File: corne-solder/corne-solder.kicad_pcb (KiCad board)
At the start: 2 copper layers, 133.8 x 91.7 mm, 49 parts, among them J1 Battery Connector, J2 nice!view, J3 USB_C_Receptacle_PowerOnly_6P, J4 Battery Wire, SW1 SW_Push, SW10 SW_Push, SW11 SW_Push, SW12 SW_Push, SW13 SW_Push, SW14 SW_Push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

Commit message: Update corne-solder.kicad_pcb
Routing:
- net GND: vias 6 -> 21
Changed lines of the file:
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@@
 		(pad_to_mask_clearance 0)
 		(allow_soldermask_bridges_in_footprints no)
-		(grid_origin 155.1 60.05)
+		(grid_origin 50 50)
 		(pcbplotparams
 			(layerselection 0x00010fc_ffffffff)
@@
 	)
 	(via
-		(at 138.5 79.125)
+		(at 126 41.75)
+		(size 0.6)
+		(drill 0.3)
+		(layers "F.Cu" "B.Cu")
+		(net 27)
+	)
+	(via
+		(at 126 79.75)
+		(size 0.6)
+		(drill 0.3)
+		(layers "F.Cu" "B.Cu")
+		(net 27)
+	)
+	(via
+		(at 145 82.125)
+		(size 0.6)
+		(drill 0.3)
+		(layers "F.Cu" "B.Cu")
+		(net 27)
+	)
+	(via
+		(at 50 65.5)
+		(size 0.6)
+		(drill 0.3)
+		(layers "F.Cu" "B.Cu")
+		(net 27)
+	)
+	(via
+		(at 69 65.5)
+		(size 0.6)
+		(drill 0.3)
+		(layers "F.Cu" "B.Cu")
+		(net 27)
+	)
+	(via
+		(at 145 44.125)
+		(size 0.6)
+		(drill 0.3)
+		(layers "F.Cu" "B.Cu")
+		(net 27)
+	)
+	(via
+		(at 145 63.125)
+		(size 0.6)
+		(drill 0.3)
+		(layers "F.Cu" "B.Cu")
+		(net 27)
+	)
+	(via
+		(at 107 39.375)
+		(size 0.6)
+		(drill 0.3)
+		(layers "F.Cu" "B.Cu")
+		(net 27)
+	)
+	(via
+		(at 50 46.5)
 		(size 0.6)
 		(drill 0.3)
@@
 	)
 	(via
-		(at 81.5 57.75)
+		(at 88 60.75)
+		(size 0.6)
+		(drill 0.3)
+		(layers "F.Cu" "B.Cu")
+		(net 27)
+	)
+	(via
+		(at 107 58.375)
+		(size 0.6)
+		(drill 0.3)
+		(layers "F.Cu" "B.Cu")
+		(net 27)
+	)
+	(via
+		(at 88 41.75)
+		(size 0.6)
+		(drill 0.3)
+		(layers "F.Cu" "B.Cu")
+		(net 27)
+	)
+	(via
+		(at 88 79.75)
+		(size 0.6)
+		(drill 0.3)
+		(layers "F.Cu" "B.Cu")
+		(net 27)
+	)
+	(via
+		(at 126 60.75)
+		(size 0.6)
+		(drill 0.3)
+		(layers "F.Cu" "B.Cu")
+		(net 27)
+	)
+	(via
+		(at 107 77.375)
+		(size 0.6)
+		(drill 0.3)
+		(layers "F.Cu" "B.Cu")
+		(net 27)
+	)
+	(via
+		(at 69 84.5)
+		(size 0.6)
+		(drill 0.3)
+		(layers "F.Cu" "B.Cu")
+		(net 27)
+	)
+	(via
+		(at 50 84.5)
 		(size 0.6)
 		(drill 0.3)
@@
 	)
 	(via
-		(at 119.5 57.75)
+		(at 69 46.5)
 		(size 0.6)
 		(drill 0.3)

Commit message: major edit
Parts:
- moved U1 0.63 mm to (164.6, 59.4)
- moved J1 0.63 mm to (162.4, 82.4)
- moved J4 0.32 mm to (157.6, 84.5)
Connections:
- U1 pad 1: unconnected-(U1-D3-TX-Pad1) -> CS
- U1 pad 12: CS -> unconnected-(U1-B5-Pad12)
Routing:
- net CS: track 22.2 -> 53.2 mm, vias 1 -> 2
- net GND: track 78.5 -> 97.8 mm, vias 21 -> 23
- net row2: track 134.7 -> 148.9 mm, vias 0 -> 1
- net row3: track 72.7 -> 86.8 mm, vias 1 -> 2
- net row0: track 121.5 -> 135.2 mm, vias 0 -> 1
- net row1: track 118.2 -> 130.6 mm, vias 0 -> 1
- net SDA: track 42.9 -> 54.5 mm
- net unconnected-(U1-D3-TX-Pad1): track 11.4 -> 0.00 mm, vias 1 -> 0
- net SCL: track 35.7 -> 45.1 mm
- net battery: track 77.1 -> 69.4 mm
- net RAW: track 22.1 -> 16.2 mm
- net VCC: track 59.9 -> 65.5 mm, vias 2 -> 4
- net col3: track 109.9 -> 106.0 mm, vias 0 -> 1
- net col2: track 114.1 -> 111.4 mm, vias 0 -> 1
- net RST: track 41.5 -> 43.0 mm
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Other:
- outline, holes or cut-outs redrawn

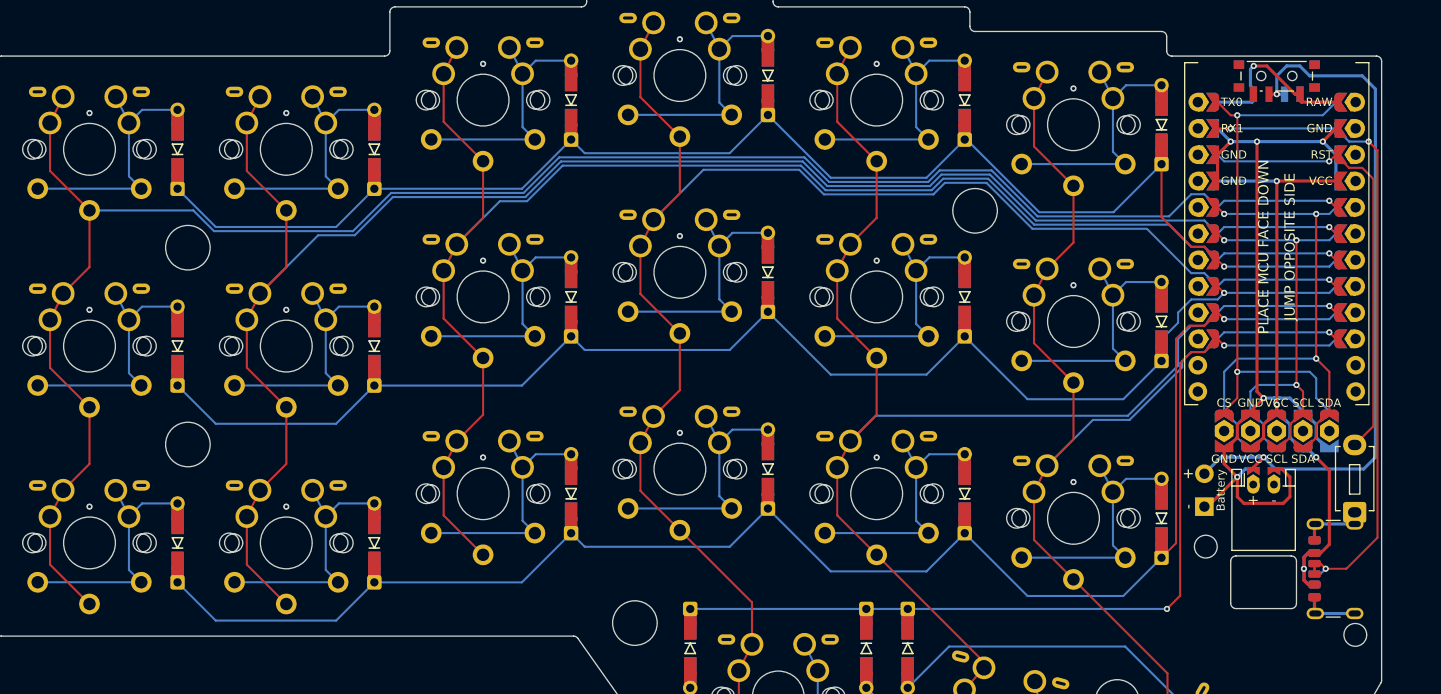
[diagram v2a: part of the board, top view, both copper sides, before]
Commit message: new design (using module)
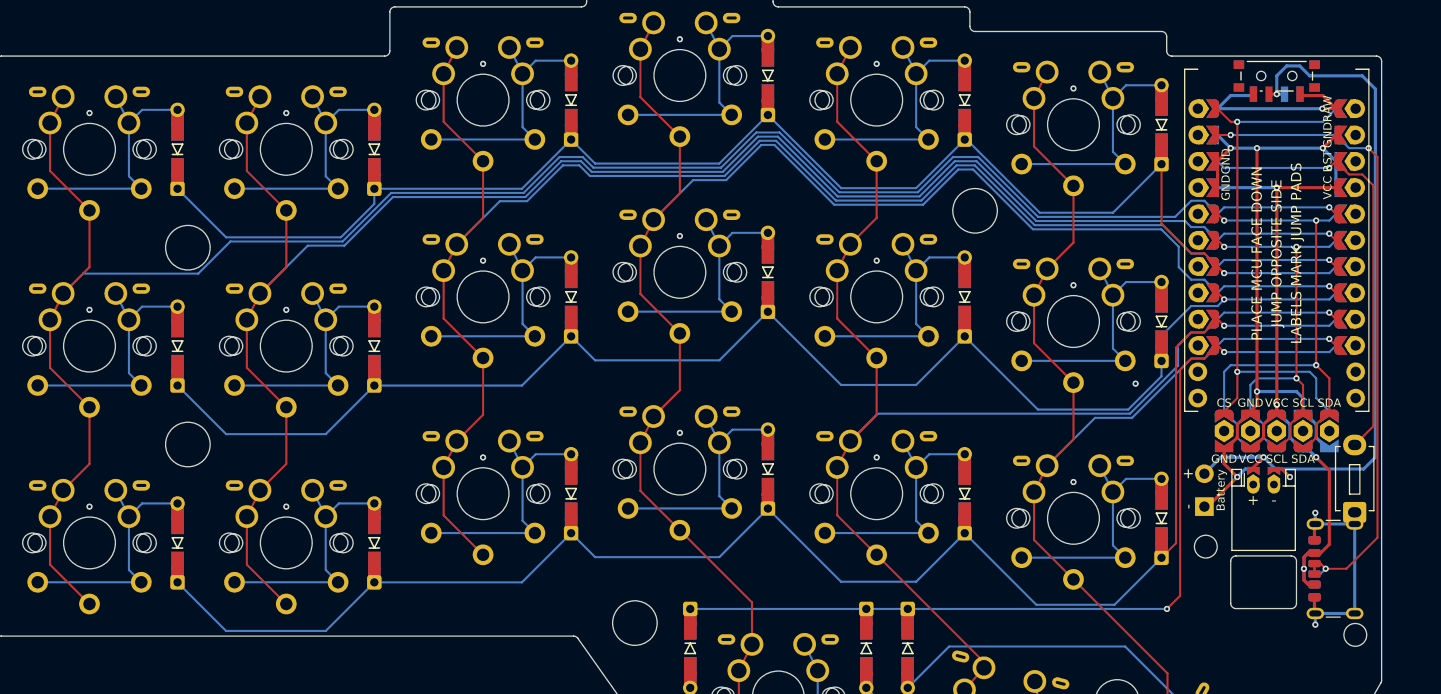
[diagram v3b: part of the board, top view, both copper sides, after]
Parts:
- moved U1 0.63 mm to (164.6, 60.0)
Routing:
- net col0: track 147.5 -> 156.2 mm
- net col3: track 106.0 -> 111.3 mm
- net col2: track 111.4 -> 116.4 mm
- net col1: track 131.6 -> 136.6 mm
- net row0: track 135.2 -> 139.2 mm
- net row1: track 130.6 -> 134.2 mm
- net RAW: track 16.2 -> 19.5 mm
- net row2: track 148.9 -> 151.3 mm
- net GND: track 97.8 -> 99.6 mm, vias 23 -> 27
- net SDA: track 54.5 -> 53.6 mm
- net col4: track 87.4 -> 86.8 mm
- net RX: track 64.5 -> 63.9 mm
- net RST: track 43.0 -> 42.3 mm
- net CS: track 53.2 -> 52.5 mm
- net row3: track 86.8 -> 86.2 mm
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
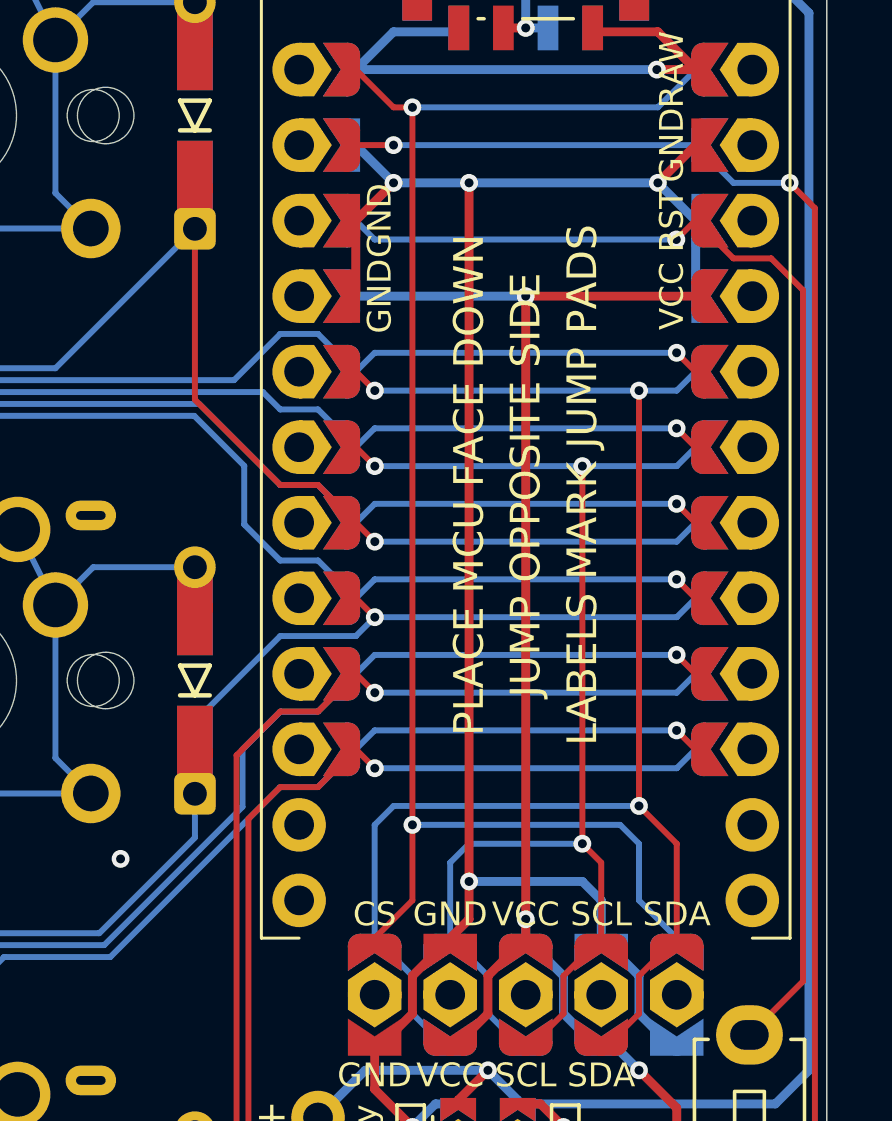
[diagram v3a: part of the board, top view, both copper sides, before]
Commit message: wiring update
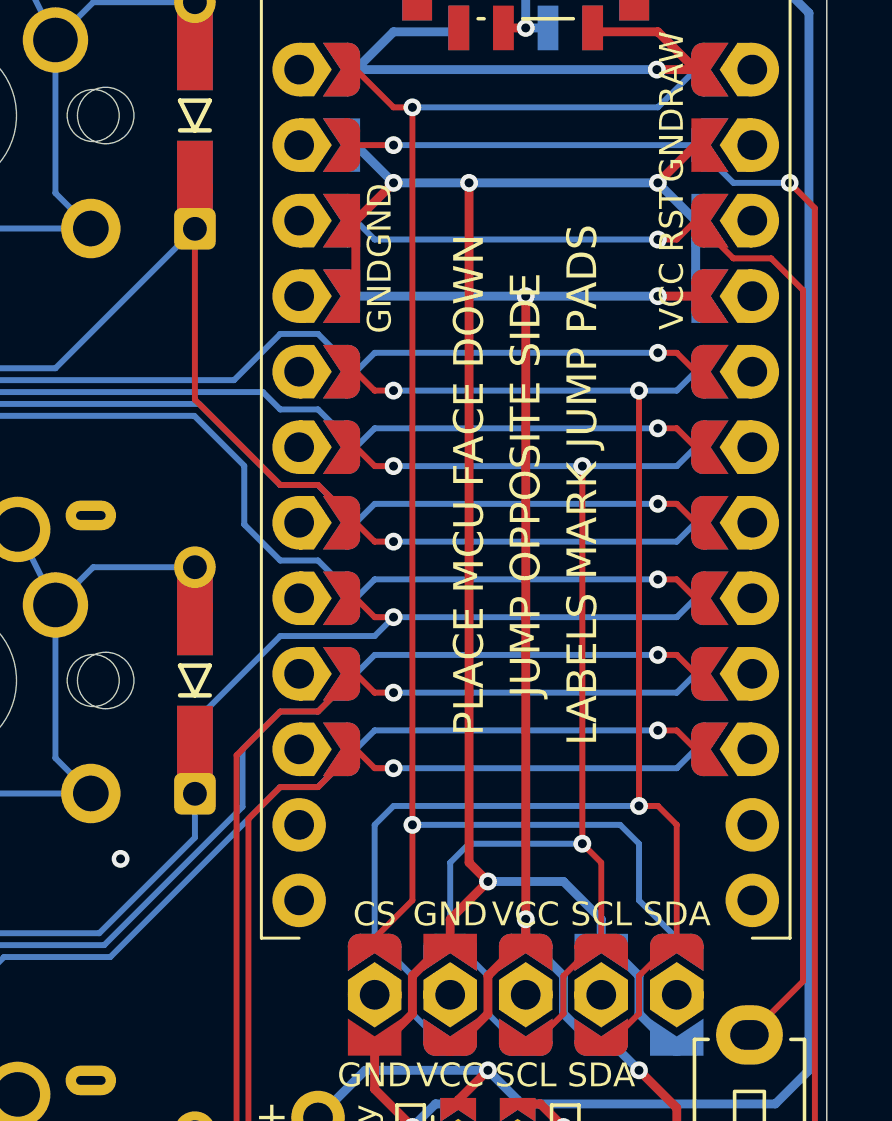
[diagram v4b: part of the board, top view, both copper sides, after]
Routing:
- net row1: track 134.2 -> 134.8 mm
- net VCC: track 64.9 -> 64.8 mm, vias 4 -> 5

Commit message: minor wiring update
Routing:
- net GND: track 99.1 -> 100.1 mm, vias 27 -> 28
- net battery: track 69.4 -> 68.9 mm

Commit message: Update corne-solder.kicad_pcb
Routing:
- net row1: track 134.8 -> 133.8 mm
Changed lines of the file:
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@@
+	)
+	(segment
+		(start 156.37 65.13)
+		(end 157.64 65.13)
+		(width 0.2)
+		(layer "F.Cu")
+		(net 4)
+	)
+	(segment
+		(start 157.64 65.13)
+		(end 158.91 63.86)
+		(width 0.2)
+		(layer "F.Cu")
+		(net 4)
 	)
 	(segment
@@
 	)
 	(segment
+		(start 153.5 68)
+		(end 156.37 65.13)
+		(width 0.2)
+		(layer "F.Cu")
+		(net 4)
+	)
+	(segment
 		(start 160.18 64.495933)
 		(end 159.545933 64.495933)
+		(width 0.2)
+		(layer "F.Cu")
+		(net 4)
+	)
+	(segment
+		(start 153.5 68.35)
+		(end 153.5 68)
 		(width 0.2)
 		(layer "F.Cu")
@@
 	)
 	(segment
-		(start 153.5 68)
-		(end 156.37 65.13)
-		(width 0.2)
-		(layer "B.Cu")
-		(net 4)
-	)
-	(segment
 		(start 153.5 70.435)
 		(end 153.5 71.909314)
@@
 		(width 0.2)
 		(layer "B.Cu")
-		(net 4)
-	)
-	(segment
-		(start 153.5 68.35)
-		(end 153.5 68)
-		(width 0.2)
-		(layer "B.Cu")
-		(net 4)
-	)
-	(segment
-		(start 159.545933 65.13)
-		(end 160.18 64.495933)
-		(width 0.2)
-		(layer "B.Cu")
-		(net 4)
-	)
-	(segment
-		(start 156.37 65.13)
-		(end 159.545933 65.13)
-		(width 0.2)
-		(layer "B.Cu")
